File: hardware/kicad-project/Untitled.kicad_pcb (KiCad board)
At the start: 2 copper layers, 110 x 70 mm, 70 parts, among them CN2 ST-0322D00-071-1A2H, J8 Conn_01x50, Q1 DMG2301L-7, Q3 DMG2301L-7, SW1 TS-1187A-B-A-B, SW10 TS-1135-C, SW2 TS-1187A-B-A-B, SW4 K2-1109SP-C4SA, SW5 K2-1109SP-C4SA, SW6 K2-1109SP-C4SA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

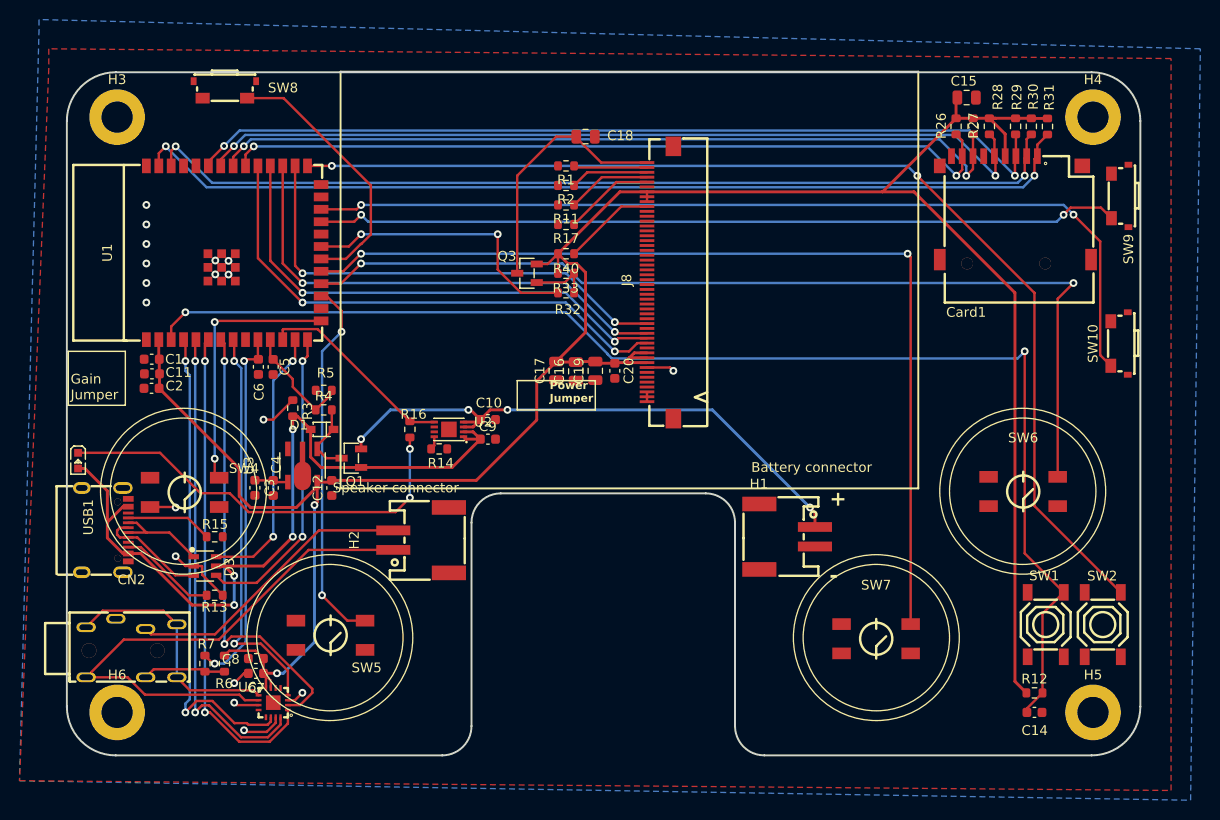
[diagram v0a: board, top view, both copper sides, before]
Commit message: New side buttons
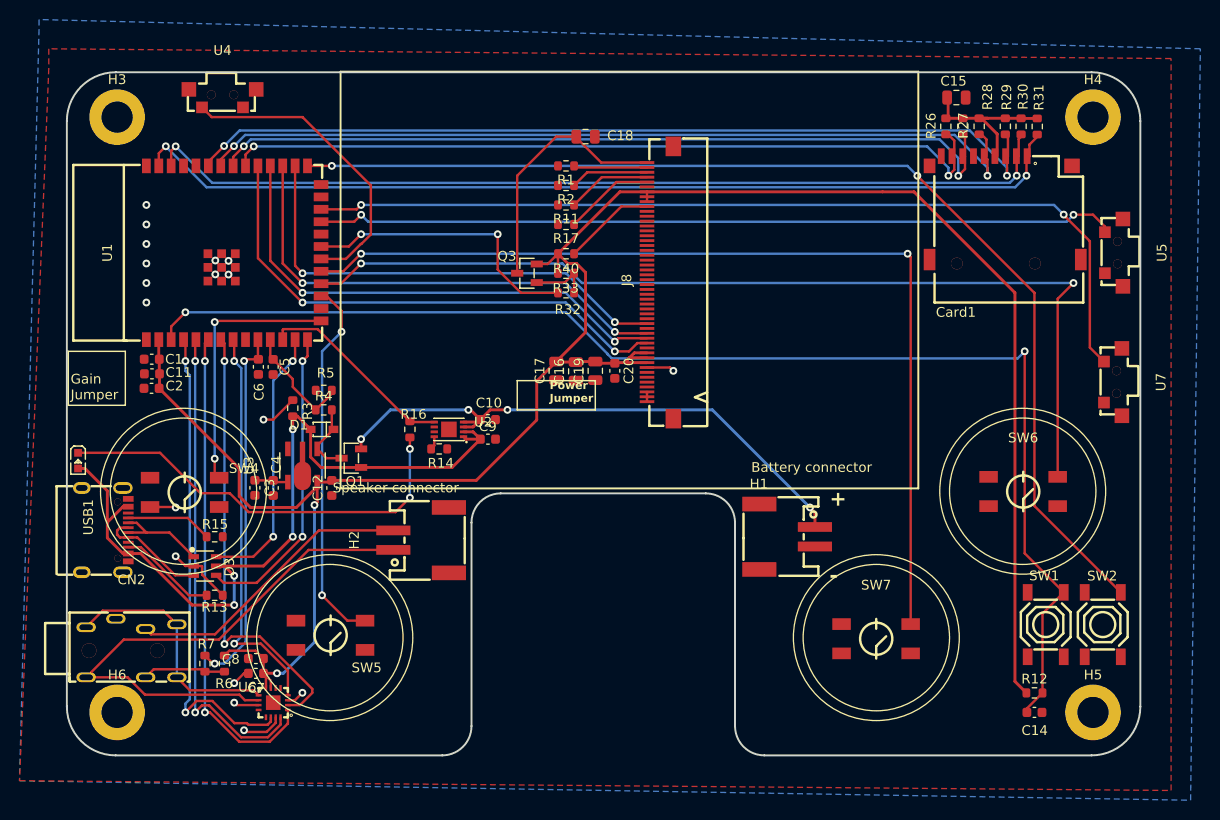
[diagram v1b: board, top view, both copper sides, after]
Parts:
- removed SW10, SW8, SW9: TS-1135-C, easyeda2kicad:SW-SMD_YIYUAN_YTS-B017-2H
- added U4: GT-TC054C-H035-L1W, easyeda2kicad:KEY-SMD_4P-L7.8-W2.8-P4.20-EH, F.Cu at (108.8, 62.1)
- added U5: GT-TC054C-H035-L1W, easyeda2kicad:KEY-SMD_4P-L7.8-W2.8-P4.20-EH, F.Cu at (200.1, 77.9)
- added U7: GT-TC054C-H035-L1W, easyeda2kicad:KEY-SMD_4P-L7.8-W2.8-P4.20-EH, F.Cu at (200.0, 91.2)
- moved C15 1.05 mm to (184.0, 62.0)
- moved Card1 1.05 mm to (189.0, 73.3)
- moved R26 1.05 mm to (182.9, 64.9)
- moved R27 1.05 mm to (184.7, 64.9)
- moved R28 1.05 mm to (186.3, 64.9)
- moved R29 1.05 mm to (189.0, 64.9)
- moved R30 1.05 mm to (190.6, 64.9)
- moved R31 1.05 mm to (192.3, 65.0)
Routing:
- net +3.3V: track 250.7 -> 240.0 mm
- net BTN_5: track 27.5 -> 31.8 mm
- net BTN_7: track 94.8 -> 93.5 mm
- net SD_DAT_3: track 95.6 -> 94.8 mm
- net SD_DAT_2: track 98.3 -> 97.6 mm

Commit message: exports
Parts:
- removed C6: 0.1uF, Capacitor_SMD:C_0603_1608Metric
- removed U4, U5, U7: GT-TC054C-H035-L1W, easyeda2kicad:KEY-SMD_4P-L7.8-W2.8-P4.20-EH
- added SW10: TS-1187A-B-A-B, easyeda2kicad:SW-SMD_4P-L5.1-W5.1-P3.70-LS6.5-TL-2, F.Cu at (199.0, 116.0)
- added SW3: K2-1109SP-C4SA, easyeda2kicad:KEY-SMD_4P-L4.5-W4.5-P3.00-LS7.0, F.Cu at (191.0, 102.5)
- added SW9: TS-1187A-B-A-B, easyeda2kicad:SW-SMD_4P-L5.1-W5.1-P3.70-LS6.5-TL-2, F.Cu at (193.0, 116.0)
- added TP1: TestPoint, TestPoint:TestPoint_Pad_D1.0mm, F.Cu at (96.0, 89.0)
- added TP2: TestPoint, TestPoint:TestPoint_Pad_D1.0mm, F.Cu at (96.0, 94.0)
- R6: value 100k -> ???k
- R7: value 100k -> 0
- SW1, SW2: value TS-1187A-B-A-B -> K2-1109SP-C4SA; footprint easyeda2kicad:SW-SMD_4P-L5.1-W5.1-P3.70-LS6.5-TL-2 -> easyeda2kicad:KEY-SMD_4P-L4.5-W4.5-P3.00-LS7.0
- SW5, SW6, SW7: value K2-1109SP-C4SA -> GT-TC054C-H035-L1W; footprint easyeda2kicad:KEY-SMD_4P-L4.5-W4.5-P3.00-LS7.0 -> easyeda2kicad:KEY-SMD_4P-L7.8-W2.8-P4.20-EH
- moved SW1 89.2 mm to (105.0, 102.5), turned to 0 degrees
- moved SW2 79.0 mm to (120.0, 117.0), turned to 0 degrees
- moved SW4 72.6 mm to (176.0, 117.0)
- moved SW5 56.1 mm to (108.9, 62.1)
- moved SW7 35.5 mm to (199.6, 91.2), turned to -90 degrees
- moved R7 30.2 mm to (98.0, 91.2), turned to 90 degrees
- moved SW6 26.4 mm to (199.6, 77.5), turned to -90 degrees
- moved R6 1.00 mm to (108.0, 120.0), turned to 90 degrees
- moved C1 0.73 mm to (101.3, 89.5)
- moved C11 0.73 mm to (101.3, 91.0)
- moved C2 0.73 mm to (101.3, 92.5)
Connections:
- CN2 pad 1: Net-(U6-OUTN) -> Net-(CN2-Pad1)
- CN2 pad 2: Net-(U6-OUTP) -> unconnected-(CN2-Pad2)
- CN2 pad 6: Net-(CN2-Pad6) -> unconnected-(CN2-Pad6)
- R6 pad 1: +3.3V -> Net-(CN2-Pad1)
- R6 pad 2: Net-(CN2-Pad6) -> Net-(U6-OUTN)
- R7 pad 1: JACK_DETECTION -> +3.3V
- R7 pad 2: Net-(CN2-Pad6) -> Net-(U1-3V3)
- SW1 pad 1: EN -> GND
- SW1 pad 3: GND -> BTN_1
- SW2 pad 1: BOOT -> GND
- SW2 pad 3: GND -> BTN_2
- SW4 pad 3: BTN_1 -> BTN_4
- SW5 pad 1: GND -> BTN_5
- SW5 pad 2: unconnected-(SW5-Pad2) -> GND
- SW5 pad 3: BTN_2 -> unconnected-(SW5-Pad3)
- SW6 pad 1: GND -> BTN_6
- SW6 pad 2: unconnected-(SW6-Pad2) -> GND
- SW6 pad 3: BTN_3 -> unconnected-(SW6-Pad3)
- SW7 pad 1: GND -> BTN_7
- SW7 pad 2: unconnected-(SW7-Pad2) -> GND
- SW7 pad 3: BTN_4 -> unconnected-(SW7-Pad3)
- U1 pad 10: JACK_DETECTION -> unconnected-(U1-IO17-Pad10)
- U1 pad 2: +3.3V -> Net-(U1-3V3)
- U1 pad 7: GAIN_CONTROL -> AMP_EN
- U1 pad 8: AMP_EN -> unconnected-(U1-IO15-Pad8)
- U6 pad 2: GAIN_CONTROL -> unconnected-(U6-GAIN_SLOT-Pad2)
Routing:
- net GAIN_CONTROL: track 46.4 -> 0.00 mm, vias 2 -> 0
- net JACK_DETECTION: track 37.9 -> 0.00 mm, vias 2 -> 0
- net Net-(U6-OUTN): track 55.5 -> 30.3 mm, vias 0 -> 2
- net Net-(CN2-Pad1): track 0.00 -> 14.1 mm
- net Net-(U1-3V3): track 0.00 -> 12.2 mm
- net Net-(CN2-Pad6): track 8.52 -> 0.00 mm
- net +3.3V: track 240.0 -> 241.2 mm
- net BTN_6: track 82.3 -> 81.3 mm
- net GND: track 27.8 -> 27.0 mm
- net AMP_EN: track 41.0 -> 41.6 mm
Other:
- board text removed: "Gain Jumper"

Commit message: update
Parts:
- C1, C10, C11, C12, C14, C2, C20, C3, C4, C5, C7, C8, C9: footprint Capacitor_SMD:C_0603_1608Metric -> Capacitor_SMD:C_0805_2012Metric
- R1, R11, R12, R13, R14, R15, R16, R17, R2, R26, R27, R28, R29, R3, R30, R31, R32, R33, R4, R40, R5, R7: footprint Resistor_SMD:R_0603_1608Metric -> Resistor_SMD:R_0805_2012Metric
- R6: value ???k -> 15k; footprint Resistor_SMD:R_0603_1608Metric -> Resistor_SMD:R_0805_2012Metric
- U1: value ESP32-S3-WROOM-1-N8 -> ESP32-S3-WROOM-1(N8R2); footprint easyeda2kicad:WIFIM-SMD_ESP32-S3-WROOM-1-N8 -> easyeda2kicad:WIRELM-SMD_ESP32-S3-WROOM-1
- moved R32 2.00 mm to (144.0, 84.0)
- moved C2 1.52 mm to (101.3, 94.0)
- moved R33 1.47 mm to (144.0, 81.5)
- moved C15 1.00 mm to (183.0, 62.0)
- moved C4 1.00 mm to (114.0, 101.0), turned to -90 degrees
- moved C3 0.99 mm to (112.0, 101.0), turned to -90 degrees
- moved R26 0.92 mm to (182.0, 64.9)
- moved C11 0.75 mm to (101.3, 91.8)
- moved R31 0.72 mm to (193.0, 65.0)
- moved C8 0.48 mm to (112.2, 119.0)
- moved R27 0.46 mm to (184.2, 64.9)
- moved R29 0.42 mm to (188.6, 64.9)
- moved C17 0.28 mm to (143.2, 90.2)
- moved C19 0.28 mm to (147.2, 90.2)
- moved C20 0.28 mm to (149.2, 90.2)
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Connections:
- U1 pad 15: BTN_1 -> unconnected-(U1-IO3-Pad15)
- U1 pad 22: unconnected-(U1-IO14-Pad22) -> BTN_1
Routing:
- net +3.3V: track 241.2 -> 254.0 mm
- net Net-(U6-OUTP): track 25.1 -> 14.6 mm
- net GND: track 27.0 -> 36.6 mm, vias 18 -> 20
- net BTN_1: track 27.4 -> 31.0 mm
- net SD_CMD: track 90.3 -> 88.3 mm
- net SD_DAT_3: track 94.8 -> 93.0 mm
- net AMP_EN: track 41.6 -> 40.3 mm
- net +5V: track 82.3 -> 83.2 mm
- net Net-(Q3-G): track 6.22 -> 7.18 mm
- net LCD_BL: track 29.4 -> 30.1 mm
- net BAT_READ: track 11.8 -> 11.2 mm
- net Net-(U1-3V3): track 12.2 -> 12.8 mm

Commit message: rev2 almost there
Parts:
- added LED1: E6C1209RGBC3UDA, easyeda2kicad:LED-ARRAY-SMD_4P-L3.2-W2.7-TL-1, F.Cu at (187.0, 89.0)
- added R10: 120, Resistor_SMD:R_0805_2012Metric, F.Cu at (182.9, 97.0)
- added R8: 30, Resistor_SMD:R_0805_2012Metric, F.Cu at (182.9, 94.0)
- added R9: 30, Resistor_SMD:R_0805_2012Metric, F.Cu at (182.9, 91.0)
- R6: value 15k -> 300
- moved TP2 1.41 mm to (95.0, 95.0)
- moved R7 1.30 mm to (97.0, 92.0)
- moved TP1 1.00 mm to (95.0, 89.0)
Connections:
- U1 pad 10: unconnected-(U1-IO17-Pad10) -> LED_RGB_GREEN
- U1 pad 8: unconnected-(U1-IO15-Pad8) -> LED_RGB_RED
- U1 pad 9: unconnected-(U1-IO16-Pad9) -> LED_RGB_BLUE
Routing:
- net LED_RGB_RED: track 0.00 -> 78.1 mm, vias 0 -> 2
- net LED_RGB_BLUE: track 0.00 -> 75.7 mm, vias 0 -> 2
- net LED_RGB_GREEN: track 0.00 -> 73.0 mm, vias 0 -> 2
- net GND: track 36.6 -> 52.2 mm, vias 20 -> 26
- net Net-(LED1-Pad1): track 0.00 -> 10.8 mm
- net +3.3V: track 254.0 -> 262.2 mm
- net Net-(LED1-Pad4): track 0.00 -> 4.74 mm
- net Net-(LED1-Pad3): track 0.00 -> 4.14 mm
- net EN: track 131.5 -> 128.6 mm
- net Net-(U1-3V3): track 12.8 -> 11.7 mm

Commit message: REV2
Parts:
- removed TP1, TP2: TestPoint, TestPoint:TestPoint_Pad_D1.0mm
- added R18: 0, Resistor_SMD:R_0805_2012Metric, F.Cu at (121.1, 125.0)
- added R19: 0, Resistor_SMD:R_0805_2012Metric, F.Cu at (175.0, 107.1)
- R6: value 300 -> 330
- moved R7 26.0 mm to (121.0, 102.0), turned to 180 degrees
- moved C12 5.00 mm to (125.0, 102.0)
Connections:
- H1 pad 1: +BATT -> Net-(H1-Pad1)
- H1 pad 4: unconnected-(H1-Pad4) -> GND
- H1 pad 5: unconnected-(H1-Pad5) -> GND
- H2 pad 4: unconnected-(H2-Pad4) -> GND
- H2 pad 5: unconnected-(H2-Pad5) -> GND
- R7 pad 2: Net-(U1-3V3) -> Net-(U3-VOUT)
- SW1 pad 2: unconnected-(SW1-Pad2) -> GND
- SW10 pad 2: unconnected-(SW10-B-Pad2) -> BOOT
- SW10 pad 4: unconnected-(SW10-D-Pad4) -> GND
- SW2 pad 2: unconnected-(SW2-Pad2) -> GND
- SW3 pad 2: unconnected-(SW3-Pad2) -> GND
- SW4 pad 2: unconnected-(SW4-Pad2) -> GND
- SW9 pad 2: unconnected-(SW9-B-Pad2) -> EN
- SW9 pad 4: unconnected-(SW9-D-Pad4) -> GND
- U1 pad 2: Net-(U1-3V3) -> +3.3V
- U3 pad 5: +3.3V -> Net-(U3-VOUT)
- U6 pad 2: unconnected-(U6-GAIN_SLOT-Pad2) -> Net-(U6-GAIN_SLOT)
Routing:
- net Net-(U1-3V3): track 11.7 -> 0.00 mm
- net Net-(H1-Pad1): track 0.00 -> 6.32 mm
- net +BATT: track 59.3 -> 65.3 mm
- net Net-(U6-GAIN_SLOT): track 0.00 -> 4.99 mm
- net Net-(CHARGE_LED1-K): track 43.3 -> 45.4 mm
- net Net-(U3-VOUT): track 0.00 -> 1.84 mm
- net +3.3V: track 262.2 -> 263.6 mm
- net GND: vias 26 -> 44

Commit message: rev 4
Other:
- board text added: "GRIGRI"

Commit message: rev2
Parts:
- removed D3: USBLC6-2SC6, easyeda2kicad:SOT-23-6_L2.9-W1.6-P0.95-LS2.8-BL
- added D2: USBLC6-2SC6_C2687116, easyeda2kicad:SOT-23-6_L2.9-W1.6-P0.95-LS2.8-BL, F.Cu at (107.2, 110.0)
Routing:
- net GND: track 52.2 -> 69.2 mm, vias 44 -> 47
- net Net-(D1-K): track 11.4 -> 24.9 mm, vias 0 -> 2
- net BOOT: track 114.3 -> 120.9 mm
- net EN: track 128.6 -> 133.1 mm
- net SD_DAT_3: track 93.0 -> 95.4 mm
- net SD_CMD: track 88.3 -> 90.4 mm

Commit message: rev2
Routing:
- net GND: track 69.2 -> 73.3 mm, vias 47 -> 49
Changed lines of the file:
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@@
   (segment (start 111.271645 119) (end 111 119) (width 0.25) (layer "F.Cu") (net 3))
   (segment (start 105 110) (end 104 109) (width 0.25) (layer "F.Cu") (net 3))
+  (segment (start 191.15 120.15) (end 192 121) (width 0.25) (layer "F.Cu") (net 3))
   (segment (start 114 100.05) (end 116.28 100.05) (width 0.25) (layer "F.Cu") (net 3))
   (segment (start 99.144549 103.12) (end 100.58 103.12) (width 0.25) (layer "F.Cu") (net 3))
@@
   (segment (start 100.2 86.8) (end 99 88) (width 0.25) (layer "F.Cu") (net 3))
   (segment (start 125 102.95) (end 123.8255 102.95) (width 0.25) (layer "F.Cu") (net 3))
+  (segment (start 191.15 112.7) (end 191.15 111.85) (width 0.25) (layer "F.Cu") (net 3))
   (segment (start 152.300185 84.157278) (end 152.300185 83.657278) (width 0.25) (layer "F.Cu") (net 3))
   (segment (start 99.144549 109.52) (end 99.144549 110.09) (width 0.25) (layer "F.Cu") (net 3))
@@
   (segment (start 121 92) (end 122 93) (width 0.25) (layer "F.Cu") (net 3))
   (segment (start 114.25 126.075) (end 114.25 125.5) (width 0.25) (layer "F.Cu") (net 3))
+  (segment (start 191.15 111.85) (end 192 111) (width 0.25) (layer "F.Cu") (net 3))
   (segment (start 108.825 113) (end 107 111.175) (width 0.25) (layer "F.Cu") (net 3))
   (segment (start 155 88.007463) (end 153.350185 89.657278) (width 0.25) (layer "F.Cu") (net 3))
   (segment (start 111.625201 126.4495) (end 111.894996 126.719295) (width 0.25) (layer "F.Cu") (net 3))
   (segment (start 111 119) (end 110 118) (width 0.25) (layer "F.Cu") (net 3))
+  (segment (start 191.15 119.3) (end 191.15 120.15) (width 0.25) (layer "F.Cu") (net 3))
   (segment (start 113.605705 126.719295) (end 114.25 126.075) (width 0.25) (layer "F.Cu") (net 3))
   (via (at 103 73) (size 0.8) (drill 0.4) (layers "F.Cu" "B.Cu") (free) (net 3))
@@
   (via (at 103 79) (size 0.8) (drill 0.4) (layers "F.Cu" "B.Cu") (free) (net 3))
   (via (at 116.987701 122.987701) (size 0.8) (drill 0.4) (layers "F.Cu" "B.Cu") (net 3))
+  (via (at 192 111) (size 0.8) (drill 0.4) (layers "F.Cu" "B.Cu") (net 3))
   (via (at 109.417545 80.134022) (size 0.8) (drill 0.4) (layers "F.Cu" "B.Cu") (free) (net 3))
   (via (at 101 79) (size 0.8) (drill 0.4) (layers "F.Cu" "B.Cu") (free) (net 3))
@@
   (via (at 103 77) (size 0.8) (drill 0.4) (layers "F.Cu" "B.Cu") (free) (net 3))
   (via (at 103 81) (size 0.8) (drill 0.4) (layers "F.Cu" "B.Cu") (free) (net 3))
+  (via (at 192 121) (size 0.8) (drill 0.4) (layers "F.Cu" "B.Cu") (net 3))
   (via (at 109 75) (size 0.8) (drill 0.4) (layers "F.Cu" "B.Cu") (free) (net 3))
   (via (at 113.547223 123.590646) (size 0.8) (drill 0.4) (layers "F.Cu" "B.Cu") (net 3))
